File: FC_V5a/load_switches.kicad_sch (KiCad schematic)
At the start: 20 parts, among them U19 AP22652, U21 AP22652, U22 AP22652, U23 AP22652, U24 AP22652

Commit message: Corrected Load Switch Erratum
The load switch current limit resistors are pulled down now instead of up!
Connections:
- net +3V3: no longer R46.1, R47.1, R48.1, R49.1, R51.1
- net GND: now also R46.1, R47.1, R48.1, R49.1, R51.1
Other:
- moved on the sheet: R46, R47, R48, R49, R51

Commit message: Updated Schematic with Burn Wire Load Switches
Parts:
- added C54, C56, C57, C58: 100nf, Capacitor_SMD:C_0402_1005Metric, symbol Adafruit ItsyBitsy RP2040-eagle-import:CAP_CERAMIC_0402NO
- added R50, R52: 10k, Resistor_SMD:R_Array_Convex_4x0603, symbol Device:R_Pack04
- added R67, R68, R76, R77, R78: 100k, Resistor_SMD:R_0603_1608Metric, symbol mainboard:R-US_R0603
- added U25, U26: AP22652, SOT26:SOT26, symbol Power_Management:AP22652
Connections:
- net +3V3: now also R50.4 (R4.1), R52.4 (R4.1), R67.1, R68.1, R76.1, R77.1, R78.1
- net GND: now also C54.2, C56.2, C57.2, C58.2, R50.6 (R3.2), R50.7 (R2.2), R52.6 (R3.2), R52.7 (R2.2), U25.2 (GND), U26.2 (GND)
- net FACE0_ENABLE renamed ~{FACE0_ENABLE}
- net ~{FACE0_ENABLE}: now also R67.2
- net FACE1_ENABLE renamed ~{FACE1_ENABLE}
- net ~{FACE1_ENABLE}: now also R68.2
- net FACE2_ENABLE renamed ~{FACE2_ENABLE}
- net ~{FACE2_ENABLE}: now also R76.2
- net FACE3_ENABLE renamed ~{FACE3_ENABLE}
- net ~{FACE3_ENABLE}: now also R78.2
- net FACE4_ENABLE renamed ~{FACE4_ENABLE}
- net ~{FACE4_ENABLE}: now also R77.2
- new net: R50.8 (R1.2), U26.5 (ILIM)
- new net: R52.1 (R1.1), R52.2 (R2.1), R52.3 (R3.1)
- new net: R52.8 (R1.2), U25.5 (ILIM)
- new net: R50.1 (R1.1), R50.2 (R2.1), R50.3 (R3.1)
- new net Burnwire Stage 1: C56.1, C57.1, U25.6 (Output), U26.1 (Input)
- new net DEPLOY1: C58.1, U26.6 (Output)
- new net VBUSP: C54.1, U25.1 (Input)
- new net ~{FIRE_DEPLOY1_A}: R52.5 (R4.2), U25.3 (EN)
- new net ~{FIRE_DEPLOY1_B}: R50.5 (R4.2), U26.3 (EN)
- no-connect marks 5 -> 7
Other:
- note added: "Enable Pull Ups Disables on Startup"
- note added: "Face Load Switches"
- note added: "This is a dumb way of getting 15k on ILIM Which results in ~1.741A Current Limit 5 Ohm Burn Resistor needs ~1.6A"
- moved on the sheet: C38, C44, C47, C48, C49, C50, C51, C52, C53, C55, R46, R47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

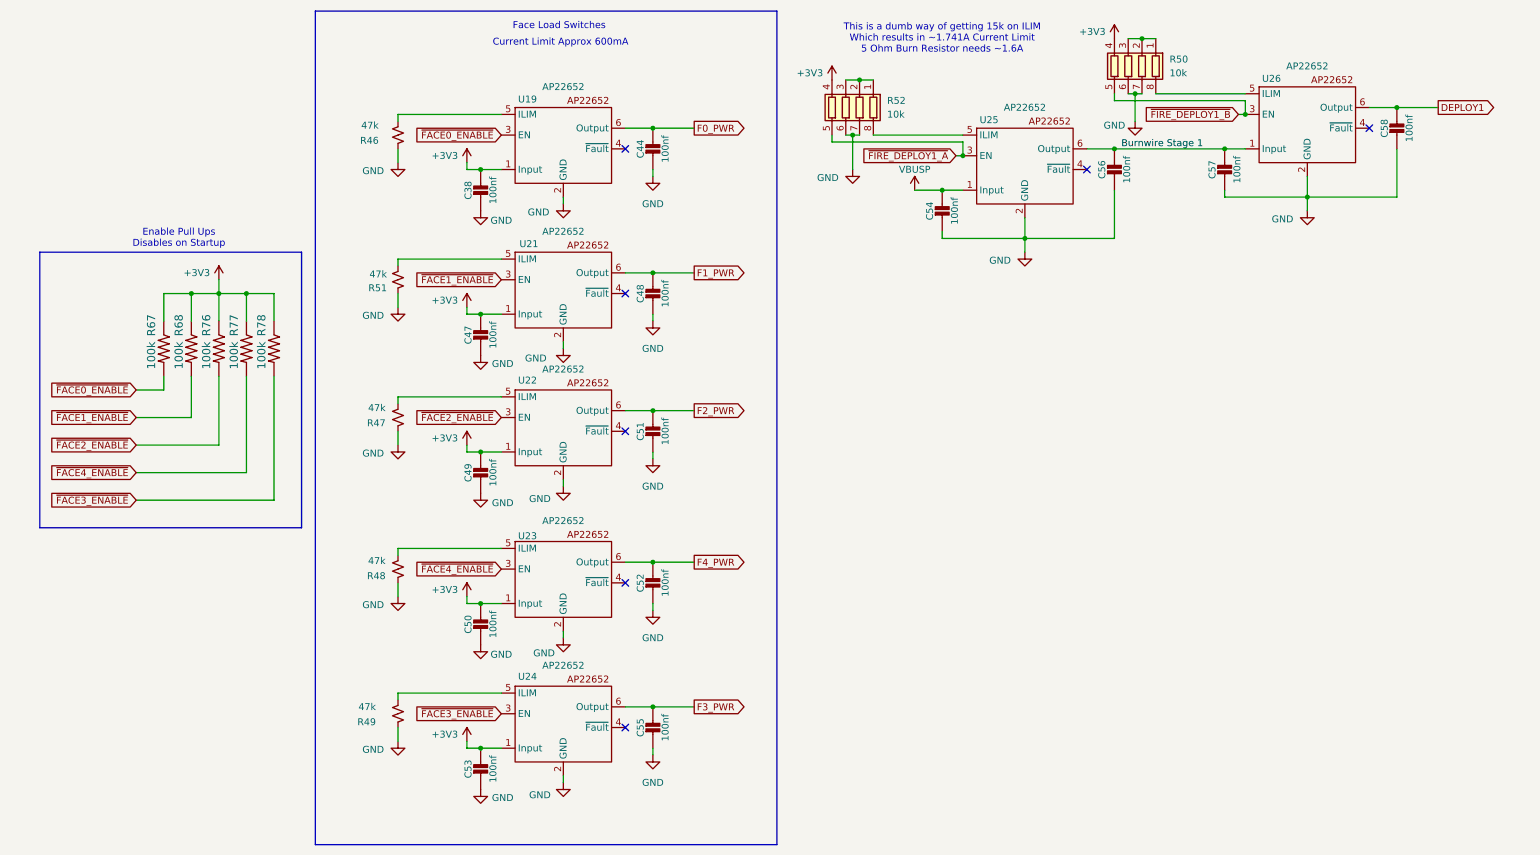
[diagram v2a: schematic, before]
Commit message: Deleted Shift Register
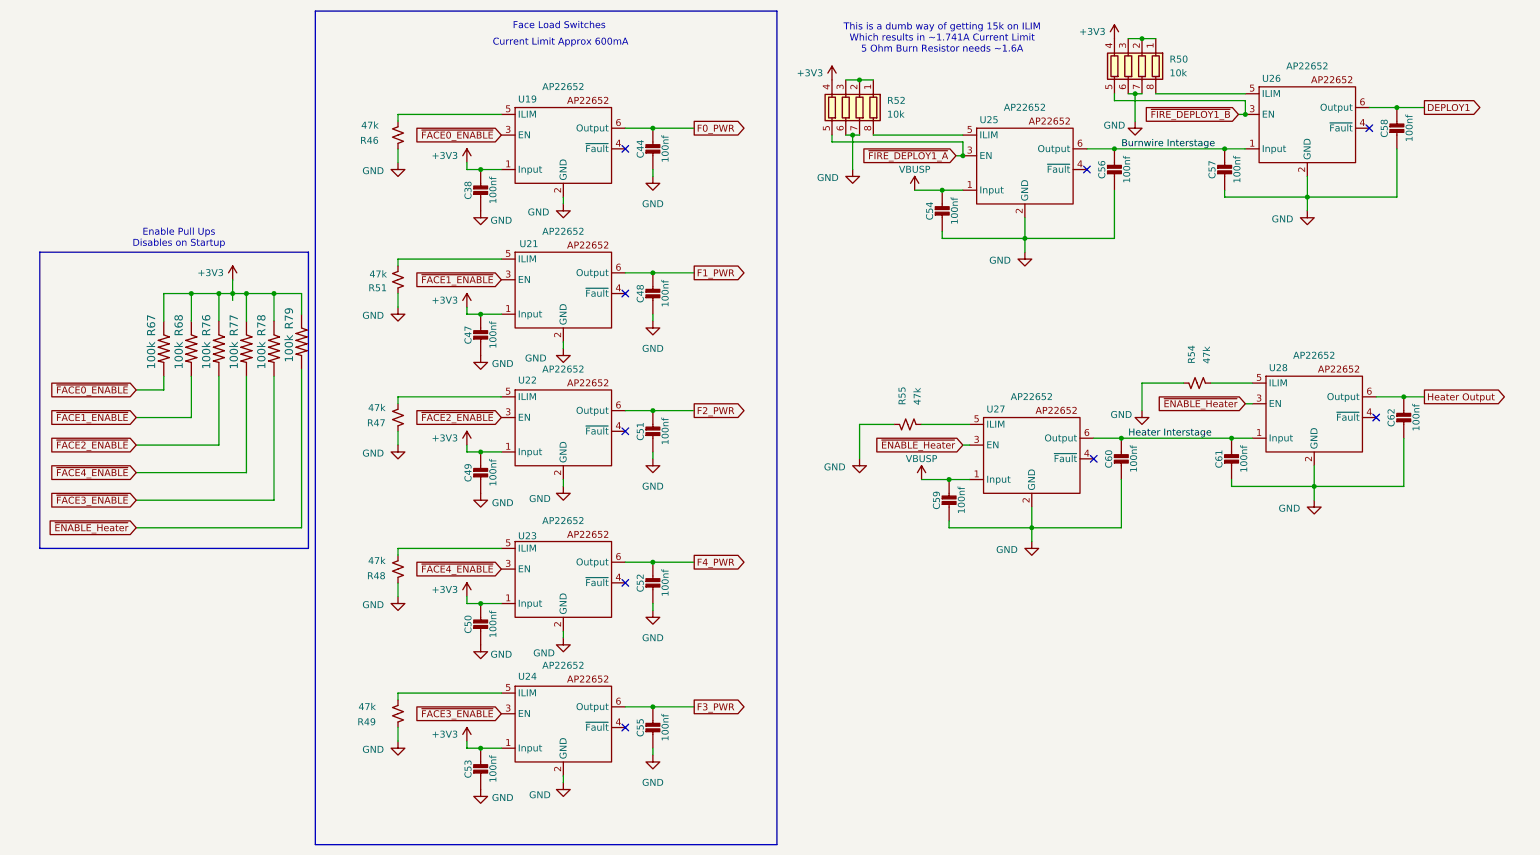
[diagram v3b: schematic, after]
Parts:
- added C59, C60, C61, C62: 100nf, Capacitor_SMD:C_0402_1005Metric, symbol Adafruit ItsyBitsy RP2040-eagle-import:CAP_CERAMIC_0402NO
- added R54, R55: 47k, Resistor_SMD:R_0603_1608Metric, symbol Device:R_Small_US
- added R79: 100k, Resistor_SMD:R_0603_1608Metric, symbol mainboard:R-US_R0603
- added U27, U28: AP22652, SOT26:SOT26, symbol Power_Management:AP22652
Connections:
- net +3V3: now also R79.1
- net GND: now also C59.2, C60.2, C61.2, C62.2, R54.1, R55.1, U27.2 (GND), U28.2 (GND)
- net VBUSP: now also C59.1, U27.1 (Input)
- net Burnwire Stage 1 renamed Burnwire Interstage
- new net: R54.2, U28.5 (ILIM)
- new net: R55.2, U27.5 (ILIM)
- new net Heater Interstage: C60.1, C61.1, U27.6 (Output), U28.1 (Input)
- new net Heater Output: C62.1, U28.6 (Output)
- new net ~{ENABLE_Heater}: R79.2, U27.3 (EN), U28.3 (EN)
- no-connect marks 7 -> 9

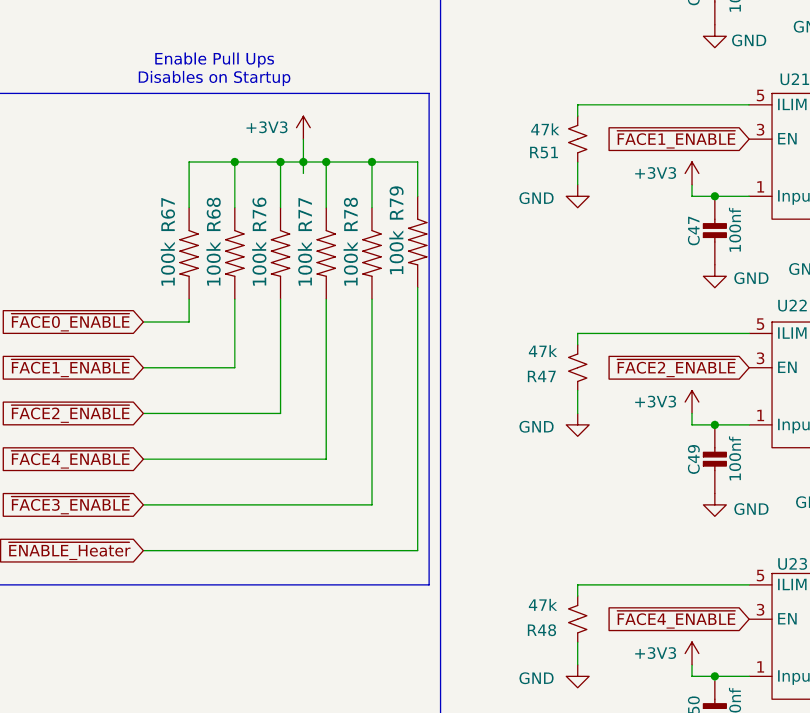
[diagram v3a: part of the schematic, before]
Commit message: Added Heater Load Switches to Schematic
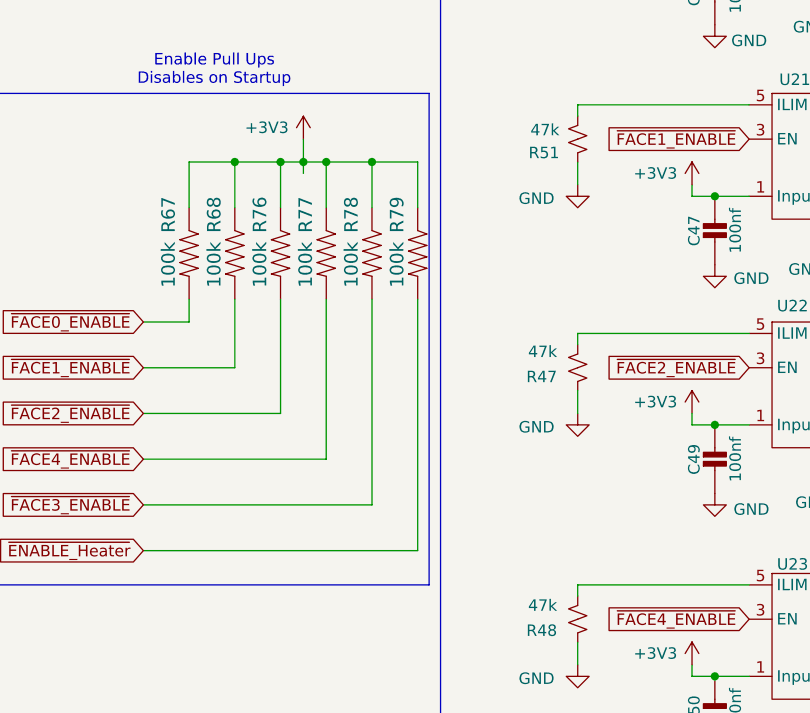
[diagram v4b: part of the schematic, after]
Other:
- moved on the sheet: R79
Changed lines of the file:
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@@
 	(wire
 		(pts
-			(xy 60.96 78.74) (xy 60.96 74.93)
+			(xy 60.96 80.01) (xy 60.96 74.93)
 		)
 		(stroke
@@
 	(wire
 		(pts
-			(xy 60.96 88.9) (xy 60.96 118.11)
+			(xy 60.96 90.17) (xy 60.96 118.11)
 		)
 		(stroke
@@
 	(symbol
 		(lib_id "mainboard:R-US_R0603")
-		(at 60.96 83.82 270)
+		(at 60.96 85.09 270)
 		(unit 1)
 		(exclude_from_sim no)
@@
 		(dnp no)
 		(property "Reference" "R79"
-			(at 58.674 81.534 0)
+			(at 58.674 82.804 0)
 			(effects
 				(font
@@
 		)
 		(property "Value" "100k"
-			(at 58.674 87.63 0)
+			(at 58.674 88.9 0)
 			(effects
 				(font
@@
 		)
 		(property "Footprint" "Resistor_SMD:R_0603_1608Metric"
-			(at 60.96 83.82 0)
+			(at 60.96 85.09 0)
 			(effects
 				(font
@@
 		)
 		(property "Datasheet" ""
-			(at 60.96 83.82 0)
+			(at 60.96 85.09 0)
 			(effects
 				(font
@@
 		)
 		(property "Description" "787K 0603"
-			(at 62.23 83.82 0)
+			(at 62.23 85.09 0)
 			(effects
 				(font

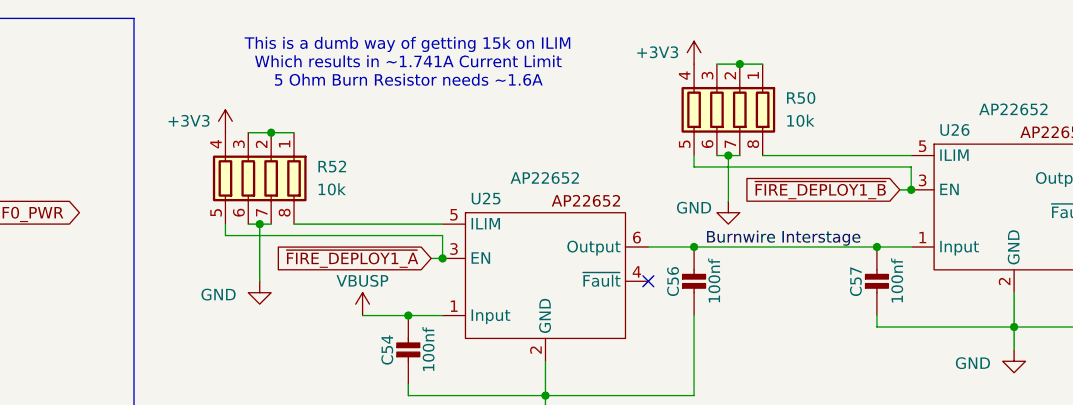
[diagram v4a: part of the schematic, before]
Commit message: Layout of New DF13 Solar Connectors
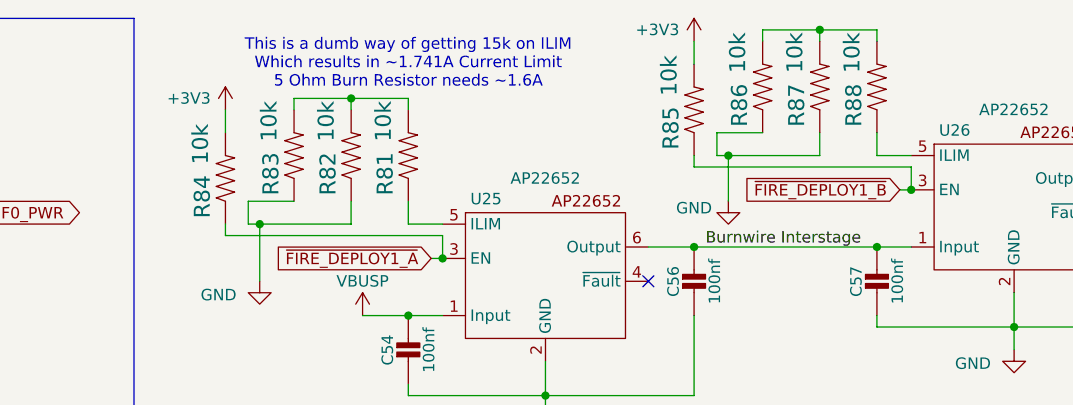
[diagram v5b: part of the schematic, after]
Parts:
- removed R50, R52: 10k, Resistor_SMD:R_Array_Convex_4x0603, symbol Device:R_Pack04
- added R81, R82, R83, R84, R85, R86, R87, R88: 10k, Resistor_SMD:R_0603_1608Metric, symbol mainboard:RESISTOR0603
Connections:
- net +3V3: now also R84.2, R85.2
- net GND: now also R82.1, R83.1, R86.1, R87.1
- net ~{FIRE_DEPLOY1_A}: now also R84.1
- net ~{FIRE_DEPLOY1_B}: now also R85.1
- net at U26.5 (ILIM): now also R88.1
- net at U25.5 (ILIM): now also R81.1
- new net: R81.2, R82.2, R83.2
- new net: R86.2, R87.2, R88.2

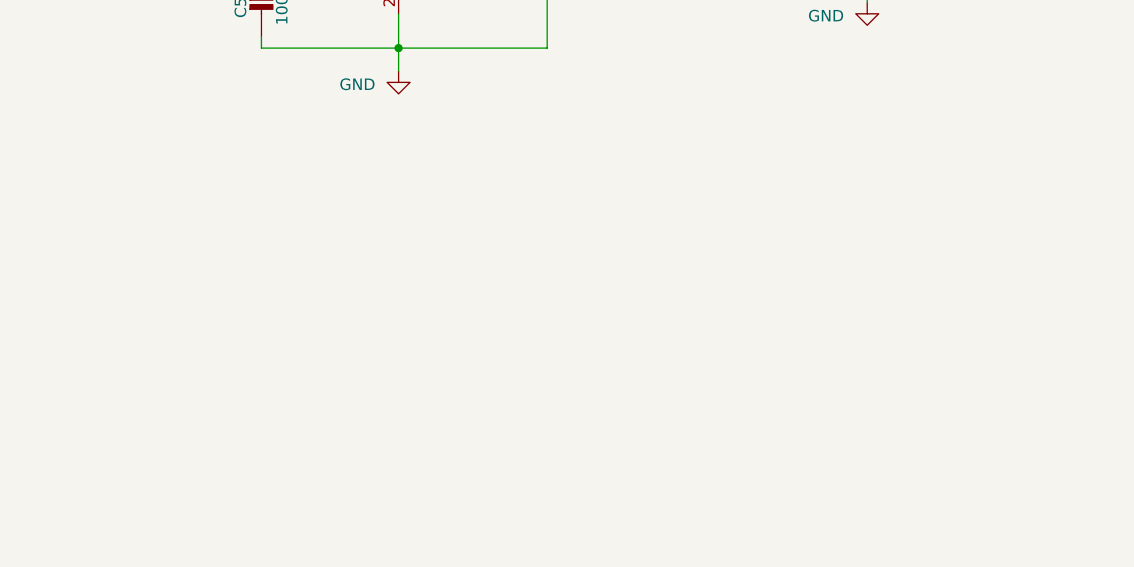
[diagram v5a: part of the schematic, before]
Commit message: Added Payload Power Load Switch
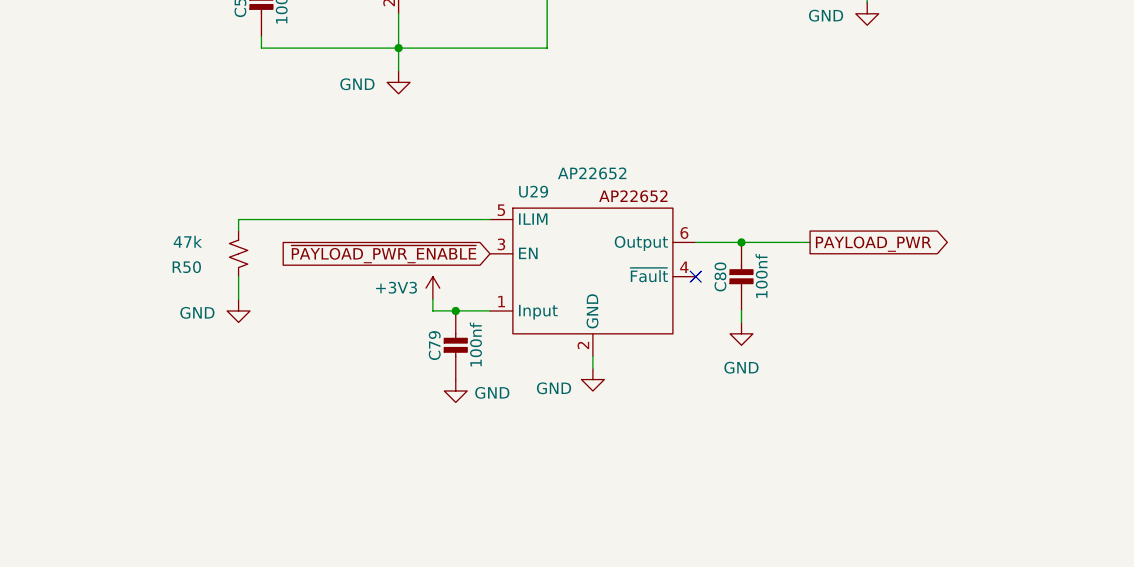
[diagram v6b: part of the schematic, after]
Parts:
- added C79, C80: 100nf, Capacitor_SMD:C_0402_1005Metric, symbol Adafruit ItsyBitsy RP2040-eagle-import:CAP_CERAMIC_0402NO
- added R50: 47k, Resistor_SMD:R_0603_1608Metric, symbol Device:R_Small_US
- added U29: AP22652, SOT26:SOT26, symbol Power_Management:AP22652
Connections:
- net +3V3: now also C79.1, U29.1 (Input)
- net GND: now also C79.2, C80.2, R50.1, U29.2 (GND)
- new net: R50.2, U29.5 (ILIM)
- new net PAYLOAD_PWR: C80.1, U29.6 (Output)
- new net ~{PAYLOAD_PWR_ENABLE}: U29.3 (EN)
- no-connect marks 9 -> 10
